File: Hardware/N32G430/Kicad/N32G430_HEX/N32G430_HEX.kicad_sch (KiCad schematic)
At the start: 2 parts

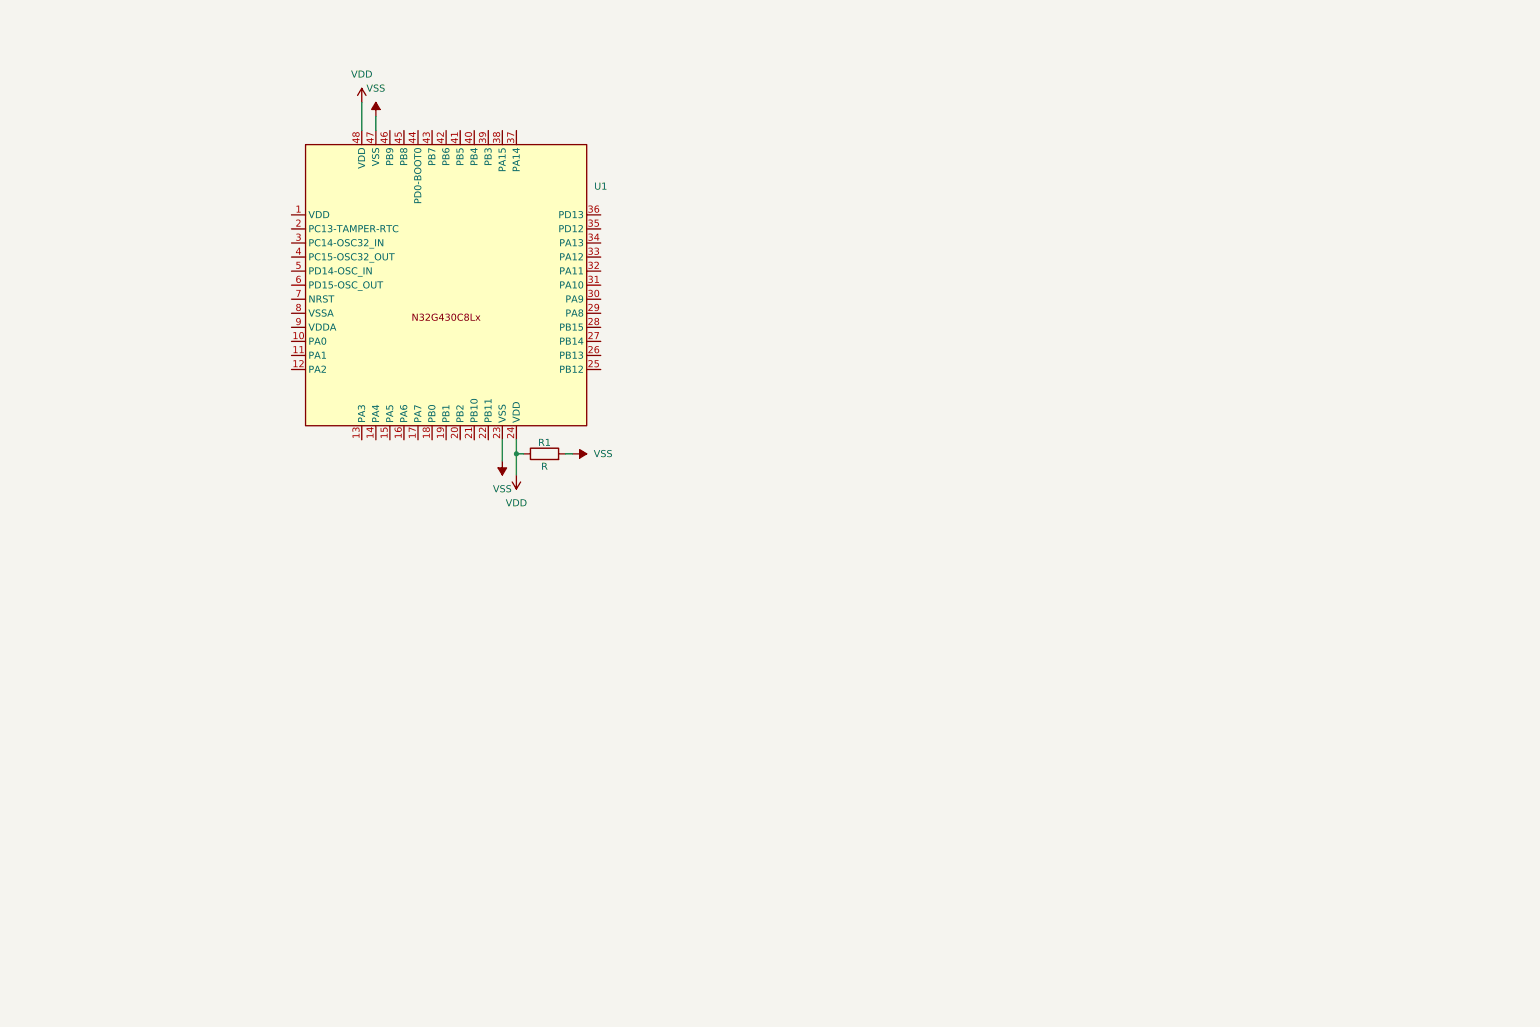
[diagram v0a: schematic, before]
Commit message: N32G430核心板绘制
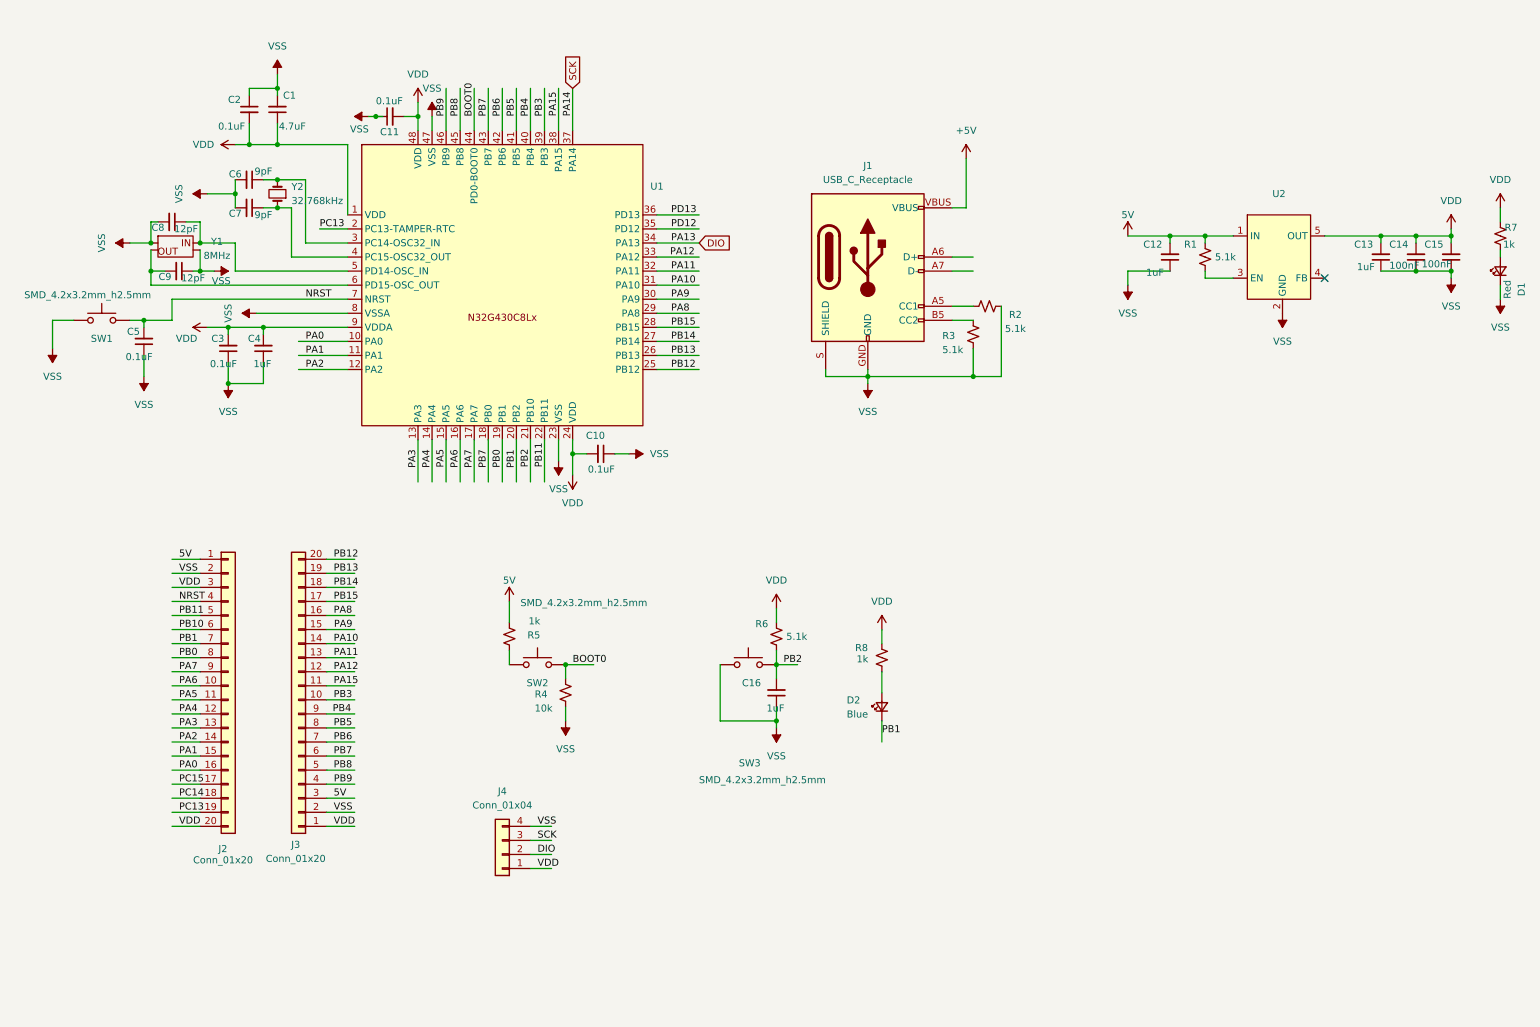
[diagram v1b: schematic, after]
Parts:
- removed R1: R, symbol Device:R
- added C1: 4.7uF, SparkFun-Capacitor:C_0603_1608Metric, symbol SparkFun-Capacitor:4.7uF_0603_35V_20%
- added C10, C11, C2, C3, C5: 0.1uF, SparkFun-Capacitor:C_0603_1608Metric, symbol SparkFun-Capacitor:0.1uF_0603_25V_20%
- added C12, C13, C16, C4: 1uF, SparkFun-Capacitor:C_0603_1608Metric, symbol SparkFun-Capacitor:0.1uF_0603_25V_20%
- added C14, C15: 100nF, SparkFun-Capacitor:C_0603_1608Metric, symbol SparkFun-Capacitor:0.1uF_0603_25V_20%
- added C6, C7: 9pF, SparkFun-Capacitor:C_0603_1608Metric, symbol SparkFun-Capacitor:1.0uF_0603_16V_10%
- added C8, C9: 12pF, SparkFun-Capacitor:C_0603_1608Metric, symbol SparkFun-Capacitor:1.0uF_0603_16V_10%
- added D1: Red, SparkFun-LED:LED_0603_1608Metric_Red, symbol SparkFun-LED:LED_Red_0603
- added D2: Blue, SparkFun-LED:LED_0603_1608Metric_Blue, symbol SparkFun-LED:LED_Blue_0603
- added J1: USB_C_Receptacle, SparkFun-Connector:USB-C_16, symbol SparkFun-Connector:USB_C_Receptacle
- added J2, J3: Conn_01x20, SparkFun-Connector:1x20, symbol SparkFun-Connector:Conn_01x20
- added J4: Conn_01x04, SparkFun-Connector:1x04, symbol SparkFun-Connector:Conn_01x04
- added R1, R2, R3, R6: 5.1k, SparkFun-Resistor:R_0603_1608Metric, symbol SparkFun-Resistor:5.1k_0603
- added R4: 10k, SparkFun-Resistor:R_0603_1608Metric, symbol SparkFun-Resistor:5.1k_0603
- added R5, R7, R8: 1k, SparkFun-Resistor:R_0603_1608Metric, symbol SparkFun-Resistor:5.1k_0603
- added SW1, SW2, SW3: SMD_4.2x3.2mm_h2.5mm, SparkFun-Switch:Push_SMD_4.2x3.2mm, symbol SparkFun-Switch:SPST_Push_SMD_4.2x3.2mm_h2.5mm
- added U2: ~, Power_BrookDawn:SGM2019, symbol Transistor_BJT:SGM2019
- added Y1: 8MHz, SparkFun-Clock:Crystal_SMD_3.2x2.5mm, symbol SparkFun-Clock:Crystal_27.12MHz_3.2x2.5mm
- added Y2: 32.768kHz, SparkFun-Clock:Crystal_SMD_3.2x1.5mm, symbol SparkFun-Clock:Crystal_32.768kHz_3.2x1.5mm
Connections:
- net VDD: now also U1.1 (VDD), U1.9 (VDDA), C1.1, C10.2, C11.2, C13.2, C14.2, C15.2, C2.2, C3.2, C4.2, J2.20 (Pin_20), J2.3 (Pin_3), J3.1 (Pin_1), J4.1 (Pin_1), R6.1, R7.1, R8.1, U2.5 (OUT)
- net VSS: now also U1.8 (VSSA), C1.2, C10.1, C11.1, C12.1, C13.1, C14.1, C15.1, C16.1, C2.1, C3.1, C4.1, C5.1, C6.2, C7.2, C8.2, C9.1, D1.1 (K), J1.GND, J1.S (SHIELD), J2.2 (Pin_2), J3.2 (Pin_2), J4.4 (Pin_4), R2.2, R3.2, R4.2, SW1.1, SW3.1, U2.2 (GND), Y1.2, Y1.4
- net PA0: now reaches U1.10 (PA0)
- net PA0: now also J2.16 (Pin_16)
- net PA1: now reaches U1.11 (PA1)
- net PA1: now also J2.15 (Pin_15)
- net PA2: now reaches U1.12 (PA2)
- net PA2: now also J2.14 (Pin_14)
- net PA3: now reaches U1.13 (PA3)
- net PA3: now also J2.13 (Pin_13)
- net PA4: now reaches U1.14 (PA4)
- net PA4: now also J2.12 (Pin_12)
- net PA5: now reaches U1.15 (PA5)
- net PA5: now also J2.11 (Pin_11)
- net PA6: now reaches U1.16 (PA6)
- net PA6: now also J2.10 (Pin_10)
- net PA7: now reaches U1.17 (PA7)
- net PA7: now also J2.9 (Pin_9)
- net PB7: now reaches U1.18 (PB0)
- net PB7: now also U1.43 (PB7), J3.6 (Pin_6)
- net PB0: now reaches U1.19 (PB1)
- net PB0: now also J2.8 (Pin_8)
- net PC13: now reaches U1.2 (PC13-TAMPER-RTC)
- net PC13: now also J2.19 (Pin_19)
- net PB1: now reaches U1.20 (PB2)
- net PB1: now also D2.1 (K), J2.7 (Pin_7)
- net PB2: now reaches U1.21 (PB10)
- net PB2: now also C16.2, R6.2, SW3.2
- net PB11: now reaches U1.22 (PB11)
- net PB11: now also J2.5 (Pin_5)
- net PB12: now reaches U1.25 (PB12)
- net PB12: now also J3.20 (Pin_20)
- net PB13: now reaches U1.26 (PB13)
- net PB13: now also J3.19 (Pin_19)
- net PB14: now reaches U1.27 (PB14)
- net PB14: now also J3.18 (Pin_18)
- net PB15: now reaches U1.28 (PB15)
- net PB15: now also J3.17 (Pin_17)
- net PA8: now reaches U1.29 (PA8)
- net PA8: now also J3.16 (Pin_16)
- net at U1.3 (PC14-OSC32_IN): now also C6.1, Y2.2
- net PA9: now reaches U1.30 (PA9)
- net PA9: now also J3.15 (Pin_15)
- net PA10: now reaches U1.31 (PA10)
- net PA10: now also J3.14 (Pin_14)
- net PA11: now reaches U1.32 (PA11)
- net PA11: now also J3.13 (Pin_13)
- net PA12: now reaches U1.33 (PA12)
- net PA12: now also J3.12 (Pin_12)
- net DIO: now reaches U1.34 (PA13)
- net DIO: now also J4.2 (Pin_2)
- net PD12: now reaches U1.35 (PD12)
- net PD13: now reaches U1.36 (PD13)
- net SCK: now reaches U1.37 (PA14)
- net SCK: now also J4.3 (Pin_3)
- net PA15: now reaches U1.38 (PA15)
- net PA15: now also J3.11 (Pin_11)
- net PB3: now reaches U1.39 (PB3)
- net PB3: now also J3.10 (Pin_10)
- net at U1.4 (PC15-OSC32_OUT): now also C7.1, Y2.1
- net PB4: now reaches U1.40 (PB4)
- net PB4: now also J3.9 (Pin_9)
- net PB5: now reaches U1.41 (PB5)
- net PB5: now also J3.8 (Pin_8)
- net PB6: now reaches U1.42 (PB6)
- net PB6: now also J3.7 (Pin_7)
- net BOOT0: now reaches U1.44 (PD0-BOOT0)
- net BOOT0: now also R4.1, SW2.2
- net PB8: now reaches U1.45 (PB8)
- net PB8: now also J3.5 (Pin_5)
- net PB9: now reaches U1.46 (PB9)
- net PB9: now also J3.4 (Pin_4)
- net at U1.5 (PD14-OSC_IN): now also C8.1, Y1.1 (OSC_IN)
- net at U1.6 (PD15-OSC_OUT): now also C9.2, Y1.3 (OSC_OUT)
- net NRST: now reaches U1.7 (NRST)
- net NRST: now also C5.2, J2.4 (Pin_4), SW1.2
- new net: J1.A5 (CC1), R2.1
- new net: J1.A6 (D+), J1.B6 (D+)
- new net: J1.A7 (D-), J1.B7 (D-)
- new net: J1.B5 (CC2), R3.1
- new net: R1.2, U2.3 (EN)
- new net: R5.1, SW2.1
- new net: D2.2 (A), R8.2
- new net: D1.2 (A), R7.2
- new net +5V: J1.VBUS
- new net 5V: C12.2, J2.1 (Pin_1), J3.3 (Pin_3), R1.1, R5.2, U2.1 (IN)
- new net PB10: J2.6 (Pin_6)
- new net PC14: J2.18 (Pin_18)
- new net PC15: J2.17 (Pin_17)
- no-connect marks 0 -> 1
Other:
- moved on the sheet: U1

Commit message: N32G430核心板绘制
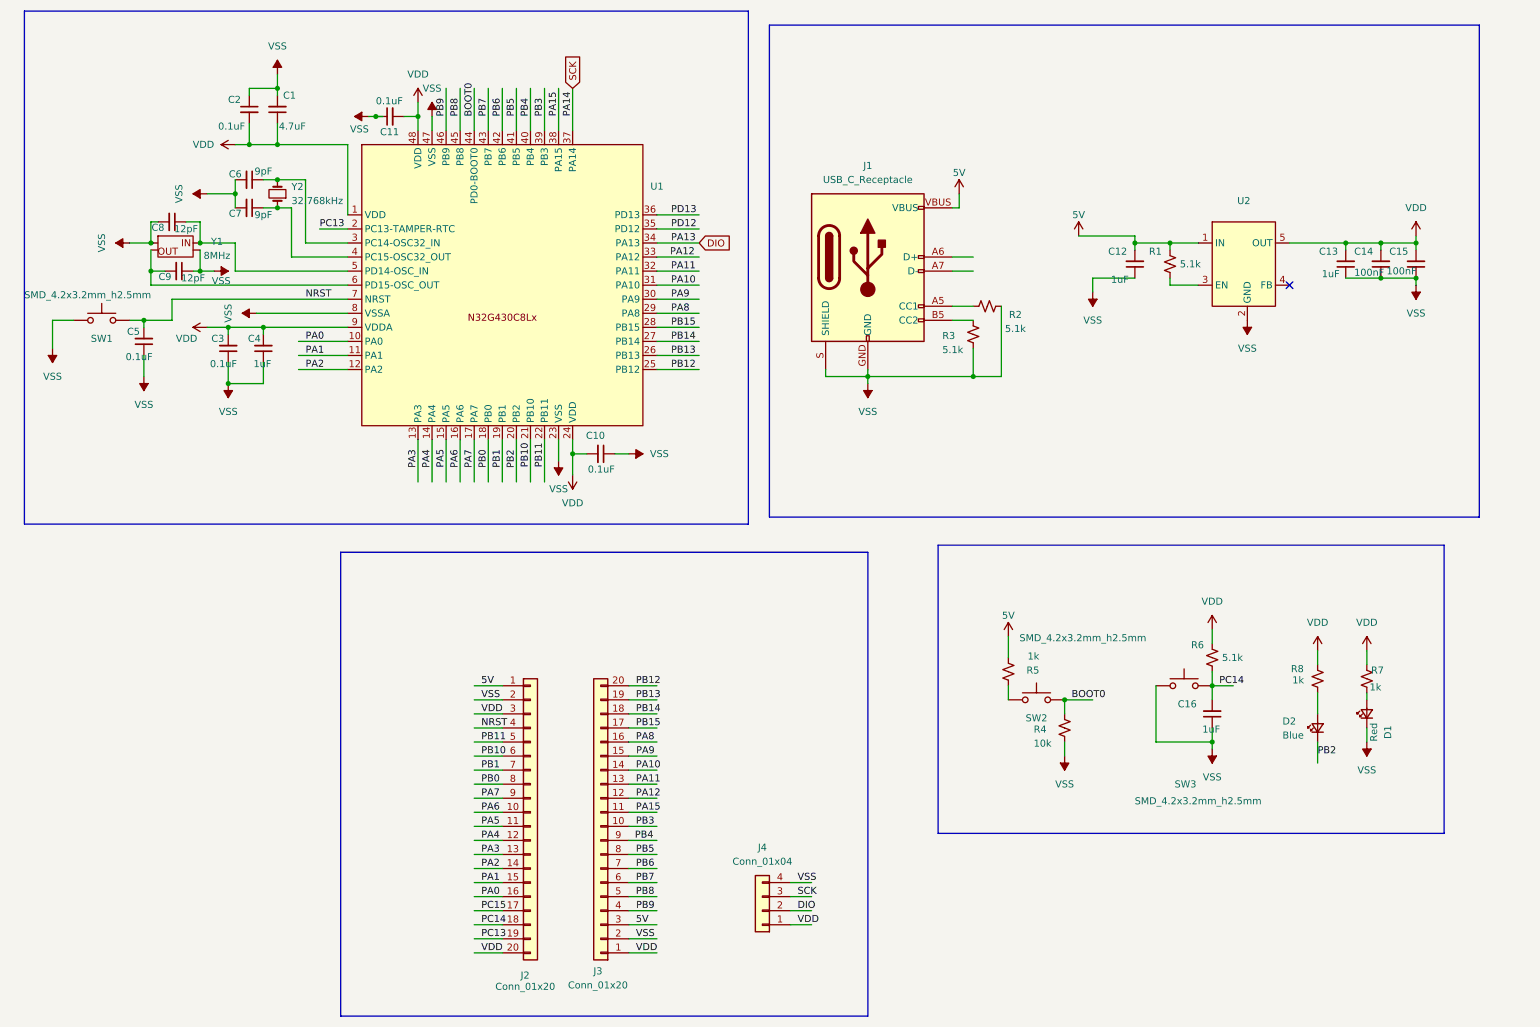
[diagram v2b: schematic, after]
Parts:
- U1: footprint N32:QFP-48_8x8_Pitch0.5mm -> N32:QFP-48_8.35x8.35_Pitch0.5mm
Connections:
- net +5V is gone; now on net 5V: J1.VBUS
- net PB0: now also U1.18 (PB0); no longer U1.19 (PB1)
- net PB1: now also U1.19 (PB1); no longer D2.1 (K), U1.20 (PB2)
- net PB10: now also U1.21 (PB10)
- net PB2: now also D2.1 (K), U1.20 (PB2); no longer C16.2, R6.2, SW3.2, U1.21 (PB10)
- net PB7: no longer U1.18 (PB0)
- net PC14: now also C16.2, R6.2, SW3.2
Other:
- moved on the sheet: C12, C13, C14, C15, C16, D1, D2, J2, J3, J4, R1, R4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
